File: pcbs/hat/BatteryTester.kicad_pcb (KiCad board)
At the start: 2 copper layers, 30 parts, among them J1 Screw_Terminal_01x02, J2 Conn_01x02_Female, J3 Conn_01x02_Female, J4 Conn_01x02_Female, J5 Conn_01x02_Female, J6 Conn_01x02_Female, J7 Conn_01x02_Female, J8 Conn_01x02_Female, J9 Conn_01x02_Female, U1 NUCLEO-F401RE, U18 MCP3008, U19 MCP3008, U20 MCP3008, U21 ???

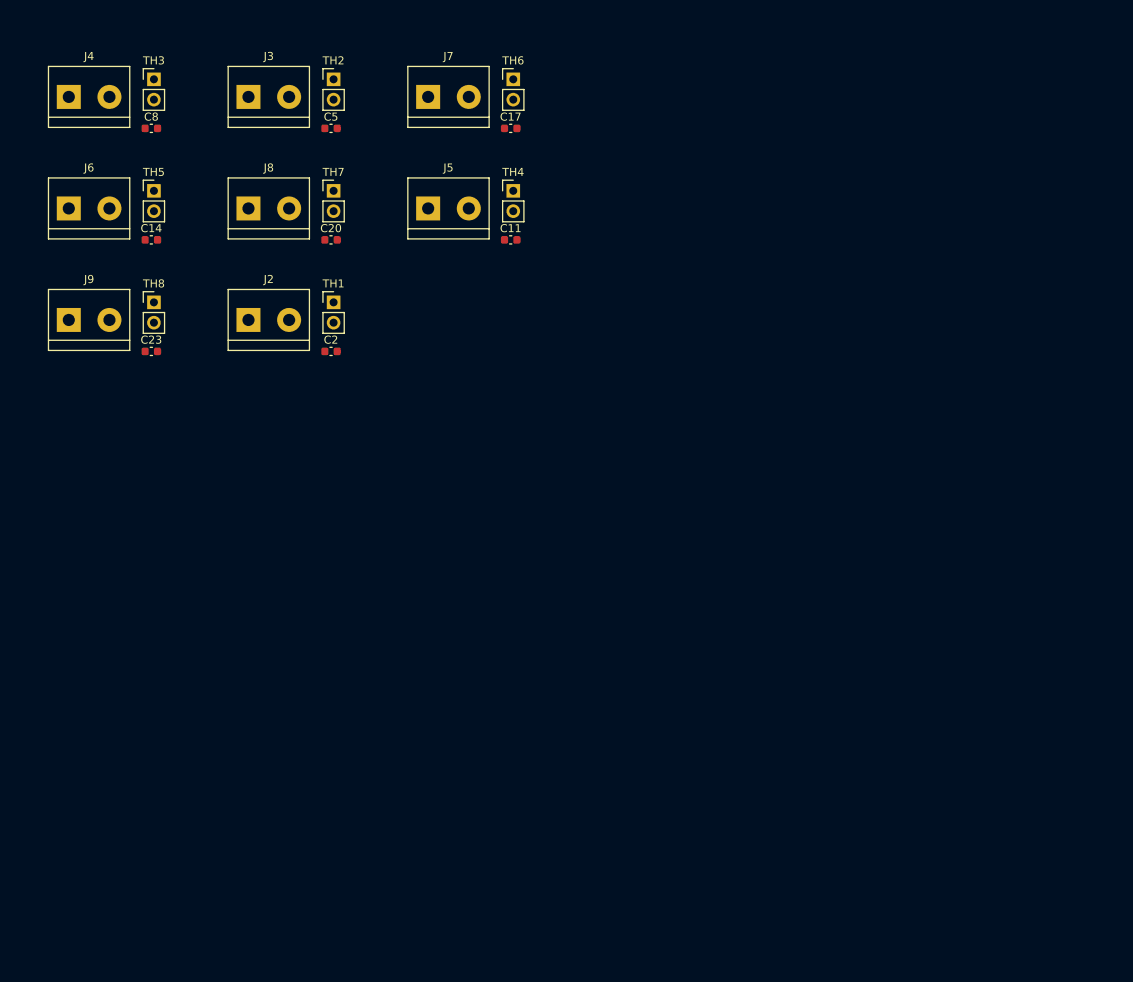
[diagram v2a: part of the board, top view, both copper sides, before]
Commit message: select parts for current and temperature sensors
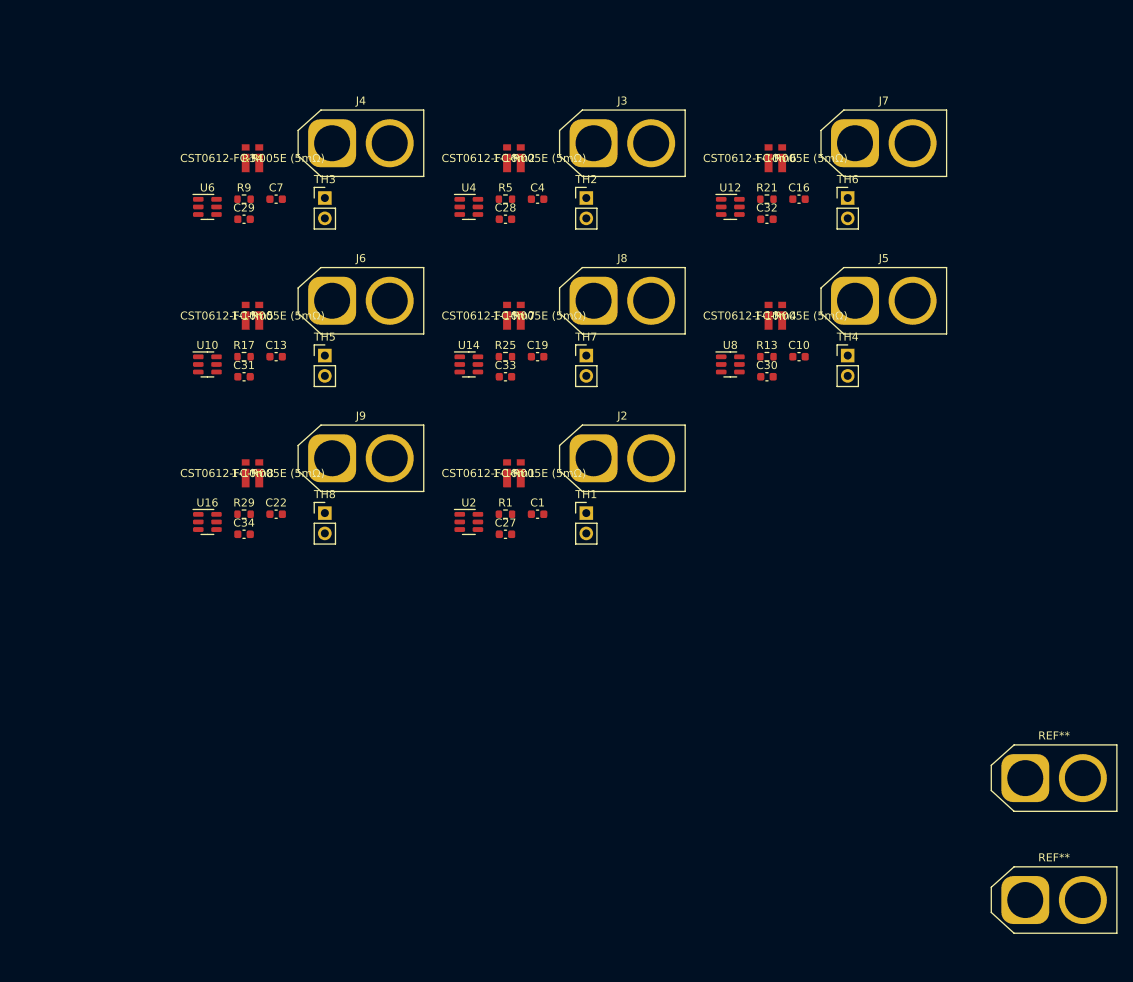
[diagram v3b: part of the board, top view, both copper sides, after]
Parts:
- removed C11, C14, C17, C2, C20, C23, C5, C8: C, Capacitor_SMD:C_0603_1608Metric
- added 1-10m1: CST0612-FC-R005E (5mΩ), STS_Resistor_SMD:CST0612-FC-R002E, F.Cu at (185.4, 83.8)
- added 1-10m2: CST0612-FC-R005E (5mΩ), STS_Resistor_SMD:CST0612-FC-R002E, F.Cu at (185.4, 44.4)
- added 1-10m4: CST0612-FC-R005E (5mΩ), STS_Resistor_SMD:CST0612-FC-R002E, F.Cu at (218.1, 64.1)
- added 1-10m5: CST0612-FC-R005E (5mΩ), STS_Resistor_SMD:CST0612-FC-R002E, F.Cu at (152.7, 64.1)
- added 1-10m6: CST0612-FC-R005E (5mΩ), STS_Resistor_SMD:CST0612-FC-R002E, F.Cu at (218.1, 44.4)
- added 1-10m7: CST0612-FC-R005E (5mΩ), STS_Resistor_SMD:CST0612-FC-R002E, F.Cu at (185.4, 64.1)
- added 1-10m8: CST0612-FC-R005E (5mΩ), STS_Resistor_SMD:CST0612-FC-R002E, F.Cu at (152.7, 83.8)
- added C1: 1µ, Capacitor_SMD:C_0603_1608Metric, F.Cu at (188.4, 88.9)
- added C10: 1µ, Capacitor_SMD:C_0603_1608Metric, F.Cu at (221.1, 69.2)
- added C13: 1µ, Capacitor_SMD:C_0603_1608Metric, F.Cu at (155.7, 69.2)
- added C16: 1µ, Capacitor_SMD:C_0603_1608Metric, F.Cu at (221.1, 49.6)
- added C19: 1µ, Capacitor_SMD:C_0603_1608Metric, F.Cu at (188.4, 69.2)
- added C22: 1µ, Capacitor_SMD:C_0603_1608Metric, F.Cu at (155.7, 88.9)
- added C27: 100n, Capacitor_SMD:C_0603_1608Metric, F.Cu at (184.4, 91.4)
- added C28: 100n, Capacitor_SMD:C_0603_1608Metric, F.Cu at (184.4, 52.1)
- added C29: 100n, Capacitor_SMD:C_0603_1608Metric, F.Cu at (151.7, 52.1)
- added C30: 100n, Capacitor_SMD:C_0603_1608Metric, F.Cu at (217.0, 71.8)
- added C31: 100n, Capacitor_SMD:C_0603_1608Metric, F.Cu at (151.7, 71.8)
- added C32: 100n, Capacitor_SMD:C_0603_1608Metric, F.Cu at (217.0, 52.1)
- added C33: 100n, Capacitor_SMD:C_0603_1608Metric, F.Cu at (184.4, 71.8)
- added C34: 100n, Capacitor_SMD:C_0603_1608Metric, F.Cu at (151.7, 91.4)
- added C4: 1µ, Capacitor_SMD:C_0603_1608Metric, F.Cu at (188.4, 49.6)
- added C7: 1µ, Capacitor_SMD:C_0603_1608Metric, F.Cu at (155.7, 49.6)
- added R1: 3k3, Resistor_SMD:R_0603_1608Metric, F.Cu at (184.4, 88.9)
- added R13: 3k3, Resistor_SMD:R_0603_1608Metric, F.Cu at (217.0, 69.2)
- added R17: 3k3, Resistor_SMD:R_0603_1608Metric, F.Cu at (151.7, 69.2)
- added R21: 3k3, Resistor_SMD:R_0603_1608Metric, F.Cu at (217.0, 49.6)
- added R25: 3k3, Resistor_SMD:R_0603_1608Metric, F.Cu at (184.4, 69.2)
- added R29: 3k3, Resistor_SMD:R_0603_1608Metric, F.Cu at (151.7, 88.9)
- added R34: CST0612-FC-R005E (5mΩ), STS_Resistor_SMD:CST0612-FC-R002E, F.Cu at (152.7, 44.4)
- added R5: 3k3, Resistor_SMD:R_0603_1608Metric, F.Cu at (184.4, 49.6)
- added R9: 3k3, Resistor_SMD:R_0603_1608Metric, F.Cu at (151.7, 49.6)
- added REF**: AMASS_XT60-F_1x02_P7.20mm_Vertical, Connector_AMASS:AMASS_XT60-F_1x02_P7.20mm_Vertical, F.Cu at (249.3, 121.9)
- added REF**: AMASS_XT60-M_1x02_P7.20mm_Vertical, Connector_AMASS:AMASS_XT60-M_1x02_P7.20mm_Vertical, F.Cu at (249.3, 137.2)
- added U10: INA181A4IDBVR, Package_TO_SOT_SMD:SOT-23-6, F.Cu at (147.1, 70.2)
- added U12: INA181A4IDBVR, Package_TO_SOT_SMD:SOT-23-6, F.Cu at (212.5, 50.5)
- added U14: INA181A4IDBVR, Package_TO_SOT_SMD:SOT-23-6, F.Cu at (179.8, 70.2)
- added U16: INA181A4IDBVR, Package_TO_SOT_SMD:SOT-23-6, F.Cu at (147.1, 89.9)
- added U2: INA181A4IDBVR, Package_TO_SOT_SMD:SOT-23-6, F.Cu at (179.8, 89.9)
- added U4: INA181A4IDBVR, Package_TO_SOT_SMD:SOT-23-6, F.Cu at (179.8, 50.5)
- added U6: INA181A4IDBVR, Package_TO_SOT_SMD:SOT-23-6, F.Cu at (147.1, 50.5)
- added U8: INA181A4IDBVR, Package_TO_SOT_SMD:SOT-23-6, F.Cu at (212.5, 70.2)
- J2, J3, J4, J5, J6, J7, J8, J9: value Conn_01x02_Female -> XT60; footprint TerminalBlock:TerminalBlock_bornier-2_P5.08mm -> Connector_AMASS:AMASS_XT60-M_1x02_P7.20mm_Vertical
- TH1, TH2, TH3, TH4, TH5, TH6, TH7, TH8: value Thermistor_NTC -> Thermistor_NTC_10k
- moved J5 54.6 mm to (228.1, 62.3)
- moved J7 53.7 mm to (228.1, 42.6)
- moved TH4 46.6 mm to (227.1, 69.1)
- moved J2 46.5 mm to (195.4, 81.9)
- moved J8 44.7 mm to (195.4, 62.3)
- moved TH6 44.4 mm to (227.1, 49.4)
- moved J3 43.5 mm to (195.4, 42.6)
- moved TH1 41.1 mm to (194.5, 88.8)
- moved TH7 37.7 mm to (194.5, 69.1)
- moved J9 37.2 mm to (162.7, 81.9)
- moved TH2 34.9 mm to (194.5, 49.4)
- moved J6 34.9 mm to (162.7, 62.3)
- moved TH8 33.9 mm to (161.8, 88.8)
- moved J4 33.4 mm to (162.7, 42.6)
- moved TH5 29.7 mm to (161.8, 69.1)
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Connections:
- J2 pad 1: Net-(1-10m1-Pad1) -> /test-battery-1/VBAT
- J2 pad 2: /test-battery-1/VBAT -> /test-battery-1/GNDBAT
- J3 pad 1: Net-(1-10m2-Pad1) -> /test-battery-2/VBAT
- J3 pad 2: /test-battery-2/VBAT -> /test-battery-2/GNDBAT
- J4 pad 1: Net-(1-10m3-Pad1) -> /test-battery-3/VBAT
- J4 pad 2: /test-battery-3/VBAT -> /test-battery-3/GNDBAT
- J5 pad 1: Net-(1-10m4-Pad1) -> /test-battery-4/VBAT
- J5 pad 2: /test-battery-4/VBAT -> /test-battery-4/GNDBAT
- J6 pad 1: Net-(1-10m5-Pad1) -> /test-battery-5/VBAT
- J6 pad 2: /test-battery-5/VBAT -> /test-battery-5/GNDBAT
- J7 pad 1: Net-(1-10m6-Pad1) -> /test-battery-8/VBAT
- J7 pad 2: /test-battery-8/VBAT -> /test-battery-8/GNDBAT
- J8 pad 1: Net-(1-10m7-Pad1) -> /test-battery-7/VBAT
- J8 pad 2: /test-battery-7/VBAT -> /test-battery-7/GNDBAT
- J9 pad 1: Net-(1-10m8-Pad1) -> /test-battery-6/VBAT
- J9 pad 2: /test-battery-6/VBAT -> /test-battery-6/GNDBAT
- U21 pad 3: unconnected-(U21-Pad3) -> GND

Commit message: work on charging circuit
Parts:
- removed REF**: AMASS_XT60-F_1x02_P7.20mm_Vertical, Connector_AMASS:AMASS_XT60-F_1x02_P7.20mm_Vertical
- removed REF**: AMASS_XT60-M_1x02_P7.20mm_Vertical, Connector_AMASS:AMASS_XT60-M_1x02_P7.20mm_Vertical
- added C12: 1µ, Capacitor_SMD:C_0603_1608Metric, F.Cu at (225.1, 83.8)
- added C15: 1µ, Capacitor_SMD:C_0603_1608Metric, F.Cu at (124.5, 83.8)
- added C18: 1µ, Capacitor_SMD:C_0603_1608Metric, F.Cu at (225.1, 53.3)
- added C21: 1µ, Capacitor_SMD:C_0603_1608Metric, F.Cu at (174.8, 83.8)
- added C24: 1µ, Capacitor_SMD:C_0603_1608Metric, F.Cu at (124.5, 114.3)
- added C3: 1µ, Capacitor_SMD:C_0603_1608Metric, F.Cu at (174.8, 114.3)
- added C6: 1µ, Capacitor_SMD:C_0603_1608Metric, F.Cu at (174.8, 53.3)
- added C9: 1µ, Capacitor_SMD:C_0603_1608Metric, F.Cu at (124.5, 53.3)
- added R11: 10k, Resistor_SMD:R_0603_1608Metric, F.Cu at (163.6, 31.9)
- added R12: 3k3, Resistor_SMD:R_0603_1608Metric, F.Cu at (163.6, 29.4)
- added R15: 10k, Resistor_SMD:R_0603_1608Metric, F.Cu at (264.2, 62.4)
- added R16: 3k3, Resistor_SMD:R_0603_1608Metric, F.Cu at (264.2, 59.9)
- added R19: 10k, Resistor_SMD:R_0603_1608Metric, F.Cu at (163.6, 62.4)
- added R20: 3k3, Resistor_SMD:R_0603_1608Metric, F.Cu at (163.6, 59.9)
- added R23: 10k, Resistor_SMD:R_0603_1608Metric, F.Cu at (264.2, 31.9)
- added R24: 3k3, Resistor_SMD:R_0603_1608Metric, F.Cu at (264.2, 29.4)
- added R27: 10k, Resistor_SMD:R_0603_1608Metric, F.Cu at (213.9, 62.4)
- added R28: 3k3, Resistor_SMD:R_0603_1608Metric, F.Cu at (213.9, 59.9)
- added R3: 10k, Resistor_SMD:R_0603_1608Metric, F.Cu at (213.9, 92.9)
- added R31: 10k, Resistor_SMD:R_0603_1608Metric, F.Cu at (163.6, 92.9)
- added R32: 3k3, Resistor_SMD:R_0603_1608Metric, F.Cu at (163.6, 90.4)
- added R35: 680, Resistor_SMD:R_0603_1608Metric, F.Cu at (209.2, 97.6)
- added R36: 10k, Resistor_SMD:R_0603_1608Metric, F.Cu at (206.6, 100.7)
- added R37: 680, Resistor_SMD:R_0603_1608Metric, F.Cu at (209.2, 36.6)
- added R38: 10k, Resistor_SMD:R_0603_1608Metric, F.Cu at (206.6, 39.7)
- added R39: 680, Resistor_SMD:R_0603_1608Metric, F.Cu at (158.9, 36.6)
- added R4: 3k3, Resistor_SMD:R_0603_1608Metric, F.Cu at (213.9, 90.4)
- added R40: 10k, Resistor_SMD:R_0603_1608Metric, F.Cu at (156.3, 39.7)
- added R41: 680, Resistor_SMD:R_0603_1608Metric, F.Cu at (259.6, 67.1)
- added R42: 10k, Resistor_SMD:R_0603_1608Metric, F.Cu at (256.9, 70.2)
- added R43: 680, Resistor_SMD:R_0603_1608Metric, F.Cu at (158.9, 67.1)
- added R44: 10k, Resistor_SMD:R_0603_1608Metric, F.Cu at (156.3, 70.2)
- added R45: 680, Resistor_SMD:R_0603_1608Metric, F.Cu at (259.6, 36.6)
- added R46: 10k, Resistor_SMD:R_0603_1608Metric, F.Cu at (256.9, 39.7)
- added R47: 680, Resistor_SMD:R_0603_1608Metric, F.Cu at (209.2, 67.1)
- added R48: 10k, Resistor_SMD:R_0603_1608Metric, F.Cu at (206.6, 70.2)
- added R49: 680, Resistor_SMD:R_0603_1608Metric, F.Cu at (158.9, 97.6)
- added R50: 10k, Resistor_SMD:R_0603_1608Metric, F.Cu at (156.3, 100.7)
- added R7: 10k, Resistor_SMD:R_0603_1608Metric, F.Cu at (213.9, 31.9)
- added R8: 3k3, Resistor_SMD:R_0603_1608Metric, F.Cu at (213.9, 29.4)
- added U11: TP5000_Breakout_Akaddy, STS_Boards:TP5000_Breakout_Akaddy, F.Cu at (126.2, 80.1)
- added U13: TP5000_Breakout_Akaddy, STS_Boards:TP5000_Breakout_Akaddy, F.Cu at (226.8, 49.6)
- added U15: TP5000_Breakout_Akaddy, STS_Boards:TP5000_Breakout_Akaddy, F.Cu at (176.5, 80.1)
- added U17: TP5000_Breakout_Akaddy, STS_Boards:TP5000_Breakout_Akaddy, F.Cu at (126.2, 110.6)
- added U3: TP5000_Breakout_Akaddy, STS_Boards:TP5000_Breakout_Akaddy, F.Cu at (176.5, 110.6)
- added U5: TP5000_Breakout_Akaddy, STS_Boards:TP5000_Breakout_Akaddy, F.Cu at (176.5, 49.6)
- added U7: TP5000_Breakout_Akaddy, STS_Boards:TP5000_Breakout_Akaddy, F.Cu at (126.2, 49.6)
- added U9: TP5000_Breakout_Akaddy, STS_Boards:TP5000_Breakout_Akaddy, F.Cu at (226.8, 80.1)
- moved TH6 37.8 mm to (259.9, 30.5)
- moved C22 35.2 mm to (132.5, 115.4)
- moved R29 34.4 mm to (128.5, 114.3)
- moved TH4 33.7 mm to (259.9, 61.0)
- moved 1-10m4 32.1 mm to (248.2, 75.3)
- moved U8 32.1 mm to (242.6, 81.4)
- moved 1-10m6 30.1 mm to (248.2, 44.8)
- moved U12 30.1 mm to (242.6, 50.9)
- moved C13 28.0 mm to (132.5, 84.9)
- moved C34 27.5 mm to (136.5, 114.3)
- moved R17 27.4 mm to (128.5, 83.8)
- moved C1 27.0 mm to (182.8, 115.4)
- moved R1 26.0 mm to (178.8, 114.3)
- moved 1-10m1 25.3 mm to (197.9, 105.8)
- moved U2 25.3 mm to (192.3, 111.9)
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
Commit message: more work on charging circuit
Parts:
- removed 1-10m1, 1-10m2, 1-10m4, 1-10m5, 1-10m6, 1-10m7, 1-10m8: CST0612-FC-R005E (5mΩ), STS_Resistor_SMD:CST0612-FC-R002E
- removed C10, C15: 1µ, Capacitor_SMD:C_0603_1608Metric
- removed C30: 100n, Capacitor_SMD:C_0603_1608Metric
- added C11: 100n, Capacitor_SMD:C_0603_1608Metric, F.Cu at (125.3, 44.5)
- added C14: 1µ, Capacitor_SMD:C_0603_1608Metric, F.Cu at (143.8, 29.8)
- added C17: 100n, Capacitor_SMD:C_0603_1608Metric, F.Cu at (239.6, 62.7)
- added C2: 100n, Capacitor_SMD:C_0603_1608Metric, F.Cu at (178.5, 98.4)
- added C23: 220u, Capacitor_THT:CP_Radial_D6.3mm_P2.50mm, F.Cu at (118.2, 78.4)
- added C26: 100n, Capacitor_SMD:C_0603_1608Metric, F.Cu at (247.5, 44.5)
- added C36: 100n, Capacitor_SMD:C_0603_1608Metric, F.Cu at (125.3, 115.8)
- added C37: 100n, Capacitor_SMD:C_0603_1608Metric, F.Cu at (117.4, 98.4)
- added C38: 220u, Capacitor_THT:CP_Radial_D6.3mm_P2.50mm, F.Cu at (118.2, 114.0)
- added C39: 1µ, Capacitor_SMD:C_0603_1608Metric, F.Cu at (143.8, 101.1)
- added C8: 220u, Capacitor_THT:CP_Radial_D6.3mm_P2.50mm, F.Cu at (179.3, 42.7)
- added Q1: Q_NMOS_DGS, Package_TO_SOT_THT:TO-220-3_Vertical, F.Cu at (194.6, 103.8)
- added Q10: Q_NMOS_DGS, Package_TO_SOT_SMD:SOT-223, F.Cu at (150.3, 58.1)
- added Q11: Q_NMOS_DGS, Package_TO_SOT_THT:TO-220-3_Vertical, F.Cu at (255.7, 32.4)
- added Q12: Q_NMOS_DGS, Package_TO_SOT_SMD:SOT-223, F.Cu at (272.5, 22.4)
- added Q13: Q_NMOS_DGS, Package_TO_SOT_THT:TO-220-3_Vertical, F.Cu at (194.6, 68.1)
- added Q14: Q_NMOS_DGS, Package_TO_SOT_SMD:SOT-223, F.Cu at (211.4, 58.1)
- added Q15: Q_NMOS_DGS, Package_TO_SOT_THT:TO-220-3_Vertical, F.Cu at (133.5, 103.8)
- added Q16: Q_NMOS_DGS, Package_TO_SOT_SMD:SOT-223, F.Cu at (150.3, 93.7)
- added Q2: Q_NMOS_DGS, Package_TO_SOT_SMD:SOT-223, F.Cu at (211.4, 93.7)
- added Q3: Q_NMOS_DGS, Package_TO_SOT_THT:TO-220-3_Vertical, F.Cu at (194.6, 32.4)
- added Q4: Q_NMOS_DGS, Package_TO_SOT_SMD:SOT-223, F.Cu at (211.4, 22.4)
- added Q5: Q_NMOS_DGS, Package_TO_SOT_THT:TO-220-3_Vertical, F.Cu at (133.5, 32.4)
- added Q6: Q_NMOS_DGS, Package_TO_SOT_SMD:SOT-223, F.Cu at (150.3, 22.4)
- added Q7: Q_NMOS_DGS, Package_TO_SOT_THT:TO-220-3_Vertical, F.Cu at (255.7, 68.1)
- added Q8: Q_NMOS_DGS, Package_TO_SOT_SMD:SOT-223, F.Cu at (272.5, 58.1)
- added Q9: Q_NMOS_DGS, Package_TO_SOT_THT:TO-220-3_Vertical, F.Cu at (133.5, 68.1)
- added R10: 1, Resistor_THT:R_Axial_DIN0617_L17.0mm_D6.0mm_P25.40mm_Horizontal, F.Cu at (161.5, 22.0)
- added R14: 10k, Resistor_SMD:R_0603_1608Metric, F.Cu at (190.4, 44.5)
- added R18: 1, Resistor_THT:R_Axial_DIN0617_L17.0mm_D6.0mm_P25.40mm_Horizontal, F.Cu at (100.4, 22.0)
- added R2: 1, Resistor_THT:R_Axial_DIN0617_L17.0mm_D6.0mm_P25.40mm_Horizontal, F.Cu at (161.5, 93.4)
- added R22: 10k, Resistor_SMD:R_0603_1608Metric, F.Cu at (129.3, 44.5)
- added R26: 1, Resistor_THT:R_Axial_DIN0617_L17.0mm_D6.0mm_P25.40mm_Horizontal, F.Cu at (222.6, 57.7)
- added R30: 10k, Resistor_SMD:R_0603_1608Metric, F.Cu at (251.5, 80.1)
- added R33: CST0612-FC-R005E (5mΩ), STS_Resistor_SMD:CST0612-FC-R002E, F.Cu at (123.6, 70.6)
- added R51: 680, Resistor_SMD:R_0603_1608Metric, F.Cu at (186.5, 62.7)
- added R52: 10k, Resistor_SMD:R_0603_1608Metric, F.Cu at (182.5, 83.5)
- added R53: 3k3, Resistor_SMD:R_0603_1608Metric, F.Cu at (178.5, 83.5)
- added R54: 10k, Resistor_SMD:R_0603_1608Metric, F.Cu at (190.4, 80.1)
- added R55: 680, Resistor_SMD:R_0603_1608Metric, F.Cu at (198.0, 71.4)
- added R56: 10k, Resistor_SMD:R_0603_1608Metric, F.Cu at (182.5, 62.7)
- added R57: CST0612-FC-R005E (5mΩ), STS_Resistor_SMD:CST0612-FC-R002E, F.Cu at (123.6, 106.3)
- added R58: 1, Resistor_THT:R_Axial_DIN0617_L17.0mm_D6.0mm_P25.40mm_Horizontal, F.Cu at (100.4, 93.4)
- added R59: 680, Resistor_SMD:R_0603_1608Metric, F.Cu at (125.4, 98.4)
- added R6: 10k, Resistor_SMD:R_0603_1608Metric, F.Cu at (190.4, 115.8)
- added R60: 10k, Resistor_SMD:R_0603_1608Metric, F.Cu at (121.4, 119.2)
- added R61: 3k3, Resistor_SMD:R_0603_1608Metric, F.Cu at (117.4, 119.2)
- added R62: 10k, Resistor_SMD:R_0603_1608Metric, F.Cu at (129.3, 115.8)
- added R63: 680, Resistor_SMD:R_0603_1608Metric, F.Cu at (136.9, 107.1)
- added R64: 10k, Resistor_SMD:R_0603_1608Metric, F.Cu at (121.4, 98.4)
- C1, C12, C16, C21, C22, C6, C7: value 1µ -> 100n
- C13, C18, C3: value 1µ -> 220u; footprint Capacitor_SMD:C_0603_1608Metric -> Capacitor_THT:CP_Radial_D6.3mm_P2.50mm
- C28, C33: value 100n -> 220u; footprint Capacitor_SMD:C_0603_1608Metric -> Capacitor_THT:CP_Radial_D6.3mm_P2.50mm
- C29, C34: value 100n -> 1µ
- R1, R17, R25, R9: value 3k3 -> CST0612-FC-R005E (5mΩ); footprint Resistor_SMD:R_0603_1608Metric -> STS_Resistor_SMD:CST0612-FC-R002E
- R11, R15, R19, R23, R27, R3, R31, R7: value 10k -> 680
- R12, R16, R20, R24, R28, R32, R4, R8: value 3k3 -> 10k
- R34: value CST0612-FC-R005E (5mΩ) -> 1; footprint STS_Resistor_SMD:CST0612-FC-R002E -> Resistor_THT:R_Axial_DIN0617_L17.0mm_D6.0mm_P25.40mm_Horizontal
- R37, R45: value 680 -> 3k3
- R41, R49: value 680 -> CST0612-FC-R005E (5mΩ); footprint Resistor_SMD:R_0603_1608Metric -> STS_Resistor_SMD:CST0612-FC-R002E
- R42, R50: value 10k -> 1; footprint Resistor_SMD:R_0603_1608Metric -> Resistor_THT:R_Axial_DIN0617_L17.0mm_D6.0mm_P25.40mm_Horizontal
- U1: value NUCLEO-F401RE -> INA181A4IDBVR; footprint STS_Boards:ST_Morpho_Connector_64_MountingHoles -> Package_TO_SOT_SMD:SOT-23-6
- U10, U12, U14, U16, U2, U4, U6, U8: value INA181A4IDBVR -> TP5000_Breakout_Akaddy; footprint Package_TO_SOT_SMD:SOT-23-6 -> STS_Boards:TP5000_Breakout_Akaddy
- U11, U13, U15, U3, U5, U7, U9: value TP5000_Breakout_Akaddy -> INA181A4IDBVR; footprint STS_Boards:TP5000_Breakout_Akaddy -> Package_TO_SOT_SMD:SOT-23-6
- U17: value TP5000_Breakout_Akaddy -> NUCLEO-F401RE; footprint STS_Boards:TP5000_Breakout_Akaddy -> STS_Boards:ST_Morpho_Connector_64_MountingHoles
- moved R24 142.9 mm to (121.4, 27.1)
- moved C29 131.7 mm to (266.0, 29.8)
- moved U1 129.1 mm to (187.0, 112.3)
- moved U11 128.1 mm to (248.1, 41.0)
- moved R23 127.3 mm to (136.9, 35.7)
- moved U7 124.9 mm to (248.1, 76.7)
- moved C12 121.8 mm to (117.4, 27.1)
- moved R29 115.3 mm to (239.6, 83.5)
- moved R21 111.9 mm to (117.4, 47.9)
- moved R37 103.2 mm to (117.4, 83.5)
- moved C27 102.0 mm to (239.6, 27.1)
- moved U9 100.9 mm to (125.9, 76.7)
- moved R31 97.9 mm to (259.1, 71.4)
- moved R43 97.3 mm to (247.6, 27.1)
- moved R35 90.8 mm to (125.4, 62.7)
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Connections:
- C1 pad 2: /SENSOR_11 -> +5V
- C12 pad 1: GND -> Net-(C12-Pad1)
- C12 pad 2: /SENSOR_40 -> GND
- C13 pad 1: GND -> Net-(C13-Pad1)
- C13 pad 2: /SENSOR_51 -> GND
- C16 pad 2: /SENSOR_81 -> +5V
- C18 pad 1: GND -> Net-(C18-Pad1)
- C18 pad 2: /SENSOR_80 -> GND
- C19 pad 2: /SENSOR_71 -> /SENSOR_41
- C21 pad 2: /SENSOR_70 -> +5V
- C22 pad 1: GND -> Net-(C22-Pad1)
- C22 pad 2: /SENSOR_61 -> GND
- C24 pad 2: /SENSOR_60 -> /SENSOR_51
- C27 pad 1: GND -> Net-(C27-Pad1)
- C27 pad 2: +5V -> GND
- C28 pad 1: GND -> Net-(C28-Pad1)
- C28 pad 2: +5V -> GND
- C29 pad 2: +5V -> /SENSOR_81
- C3 pad 1: GND -> Net-(C3-Pad1)
- C3 pad 2: /SENSOR_10 -> GND
- C32 pad 1: GND -> Net-(C32-Pad1)
- C32 pad 2: +5V -> GND
- C33 pad 1: GND -> Net-(C33-Pad1)
- C33 pad 2: +5V -> GND
- C34 pad 2: +5V -> /SENSOR_71
- C4 pad 2: /SENSOR_21 -> /SENSOR_11
- C6 pad 2: /SENSOR_20 -> +5V
- C7 pad 1: GND -> Net-(C7-Pad1)
- C7 pad 2: /SENSOR_31 -> GND
- C9 pad 2: /SENSOR_30 -> /SENSOR_21
- R1 pad 1: Net-(R1-Pad1) -> /test-battery-1/GNDBAT
- R1 pad 2: /SENSOR_11 -> Net-(R1-Pad2)
- R11 pad 1: /SENSOR_32 -> /SIGNAL_21
- R11 pad 2: GND -> Net-(C7-Pad1)
- R12 pad 1: /test-battery-3/VBAT -> Net-(C7-Pad1)
- R12 pad 2: /SENSOR_30 -> GND
- R13 pad 2: /SENSOR_41 -> /SENSOR_21
- R15 pad 1: /SENSOR_42 -> /SIGNAL_20
- R15 pad 2: GND -> Net-(Q4-Pad2)
- R16 pad 1: /test-battery-4/VBAT -> Net-(Q4-Pad2)
- R16 pad 2: /SENSOR_40 -> GND
- R17 pad 1: Net-(R17-Pad1) -> /test-battery-3/GNDBAT
- R17 pad 2: /SENSOR_51 -> Net-(R17-Pad2)
- R19 pad 1: /SENSOR_52 -> /SIGNAL_31
- R19 pad 2: GND -> Net-(C12-Pad1)
- R20 pad 1: /test-battery-5/VBAT -> Net-(C12-Pad1)
- R20 pad 2: /SENSOR_50 -> GND
- R21 pad 2: /SENSOR_81 -> /SENSOR_31
- R23 pad 1: /SENSOR_82 -> /SIGNAL_30
- R23 pad 2: GND -> Net-(Q6-Pad2)
- R24 pad 1: /test-battery-8/VBAT -> Net-(Q6-Pad2)
- R24 pad 2: /SENSOR_80 -> GND
- R25 pad 1: Net-(R25-Pad1) -> /test-battery-4/GNDBAT
- R25 pad 2: /SENSOR_71 -> Net-(R25-Pad2)
- R27 pad 1: /SENSOR_72 -> /SIGNAL_41
- R27 pad 2: GND -> Net-(C17-Pad1)
- R28 pad 1: /test-battery-7/VBAT -> Net-(C17-Pad1)
- R28 pad 2: /SENSOR_70 -> GND
- R29 pad 2: /SENSOR_61 -> /SENSOR_41
- R3 pad 1: /SENSOR_12 -> /SIGNAL_11
- R3 pad 2: GND -> Net-(C2-Pad1)
- R31 pad 1: /SENSOR_62 -> /SIGNAL_40
- R31 pad 2: GND -> Net-(Q8-Pad2)
- R32 pad 1: /test-battery-6/VBAT -> Net-(Q8-Pad2)
- R32 pad 2: /SENSOR_60 -> GND
- R34 pad 1: /test-battery-3/GNDBAT -> Net-(C23-Pad1)
- R34 pad 2: Net-(R34-Pad2) -> /test-battery-5/VBAT
- R35 pad 1: /SIGNAL_10 -> /SIGNAL_51
- R35 pad 2: Net-(Q1-Pad2) -> Net-(C22-Pad1)
- R36 pad 1: Net-(Q1-Pad2) -> Net-(C22-Pad1)
- R37 pad 1: /SIGNAL_20 -> Net-(R37-Pad1)
- R37 pad 2: Net-(Q3-Pad2) -> /SENSOR_51
- R38 pad 1: Net-(Q3-Pad2) -> /SENSOR_52
- R39 pad 1: /SIGNAL_30 -> /SIGNAL_50
- R4 pad 1: /test-battery-1/VBAT -> Net-(C2-Pad1)
- R4 pad 2: /SENSOR_10 -> GND
- R41 pad 1: /SIGNAL_40 -> /test-battery-8/GNDBAT
- R41 pad 2: Net-(Q7-Pad2) -> Net-(R41-Pad2)
- R42 pad 1: Net-(Q7-Pad2) -> Net-(C28-Pad1)
- R42 pad 2: GND -> /test-battery-8/VBAT
- R43 pad 1: /SIGNAL_50 -> /SIGNAL_81
- R43 pad 2: Net-(Q9-Pad2) -> Net-(C27-Pad1)
- R44 pad 1: Net-(Q9-Pad2) -> Net-(C27-Pad1)
- R45 pad 1: /SIGNAL_80 -> Net-(R45-Pad1)
- R45 pad 2: Net-(Q11-Pad2) -> /SENSOR_81
- R46 pad 1: Net-(Q11-Pad2) -> /SENSOR_82
- R47 pad 1: /SIGNAL_70 -> /SIGNAL_80
- R49 pad 1: /SIGNAL_60 -> /test-battery-7/GNDBAT
- R49 pad 2: Net-(Q15-Pad2) -> Net-(R49-Pad2)
- R5 pad 2: /SENSOR_21 -> /SENSOR_11
- R50 pad 1: Net-(Q15-Pad2) -> Net-(C33-Pad1)
- R50 pad 2: GND -> /test-battery-7/VBAT
- R7 pad 1: /SENSOR_22 -> /SIGNAL_10
- R7 pad 2: GND -> Net-(Q2-Pad2)
- R8 pad 1: /test-battery-2/VBAT -> Net-(Q2-Pad2)
- R8 pad 2: /SENSOR_20 -> GND
- R9 pad 1: Net-(R9-Pad1) -> /test-battery-2/GNDBAT
- R9 pad 2: /SENSOR_31 -> Net-(R9-Pad2)
- U10 pad 1: Net-(R17-Pad1) -> VCC
- U10 pad 2: GND -> Net-(Q10-Pad1)
- U10 pad 3: Net-(1-10m5-Pad2) -> /test-battery-5/VBAT
- U10 pad 4: Net-(1-10m5-Pad3) -> Net-(Q10-Pad1)
- U11 pad 1: VCC -> Net-(R45-Pad1)
- U11 pad 2: Net-(Q9-Pad1) -> GND
- U11 pad 3: /test-battery-5/VBAT -> Net-(R41-Pad2)
- U11 pad 4: Net-(Q9-Pad1) -> Net-(R41-Pad3)
- U12 pad 1: Net-(R21-Pad1) -> VCC
- U12 pad 2: GND -> Net-(Q12-Pad1)
- U12 pad 3: Net-(1-10m6-Pad2) -> /test-battery-8/VBAT
- U12 pad 4: Net-(1-10m6-Pad3) -> Net-(Q12-Pad1)
- U13 pad 1: VCC -> Net-(R53-Pad1)
- U13 pad 2: Net-(Q11-Pad1) -> GND
- U13 pad 3: /test-battery-8/VBAT -> Net-(R49-Pad2)
- U13 pad 4: Net-(Q11-Pad1) -> Net-(R49-Pad3)
- U14 pad 1: Net-(R25-Pad1) -> VCC
- U14 pad 2: GND -> Net-(Q14-Pad1)
- U14 pad 3: Net-(1-10m7-Pad2) -> /test-battery-7/VBAT
- U14 pad 4: Net-(1-10m7-Pad3) -> Net-(Q14-Pad1)
- U15 pad 1: VCC -> Net-(R61-Pad1)
- U15 pad 2: Net-(Q13-Pad1) -> GND
- U15 pad 3: /test-battery-7/VBAT -> Net-(R57-Pad2)
- U15 pad 4: Net-(Q13-Pad1) -> Net-(R57-Pad3)
- U16 pad 1: Net-(R29-Pad1) -> VCC
- U16 pad 2: GND -> Net-(Q16-Pad1)
- U16 pad 3: Net-(1-10m8-Pad2) -> /test-battery-6/VBAT
- U16 pad 4: Net-(1-10m8-Pad3) -> Net-(Q16-Pad1)
- U2 pad 1: Net-(R1-Pad1) -> VCC
- U2 pad 2: GND -> Net-(Q2-Pad1)
- U2 pad 3: Net-(1-10m1-Pad2) -> /test-battery-1/VBAT
- U2 pad 4: Net-(1-10m1-Pad3) -> Net-(Q2-Pad1)
- U3 pad 1: VCC -> Net-(R13-Pad1)
- U3 pad 2: Net-(Q1-Pad1) -> GND
- U3 pad 3: /test-battery-1/VBAT -> Net-(R9-Pad2)
- U3 pad 4: Net-(Q1-Pad1) -> Net-(R9-Pad3)
- U4 pad 1: Net-(R5-Pad1) -> VCC
- U4 pad 2: GND -> Net-(Q4-Pad1)
- U4 pad 3: Net-(1-10m2-Pad2) -> /test-battery-2/VBAT
- U4 pad 4: Net-(1-10m2-Pad3) -> Net-(Q4-Pad1)
- U5 pad 1: VCC -> Net-(R21-Pad1)
- U5 pad 2: Net-(Q3-Pad1) -> GND
- U5 pad 3: /test-battery-2/VBAT -> Net-(R17-Pad2)
- U5 pad 4: Net-(Q3-Pad1) -> Net-(R17-Pad3)
- U6 pad 1: Net-(R9-Pad1) -> VCC
- U6 pad 2: GND -> Net-(Q6-Pad1)
- U6 pad 3: Net-(R34-Pad2) -> /test-battery-3/VBAT
- U6 pad 4: Net-(R34-Pad3) -> Net-(Q6-Pad1)
- U7 pad 1: VCC -> Net-(R29-Pad1)
- U7 pad 2: Net-(Q5-Pad1) -> GND
- U7 pad 3: /test-battery-3/VBAT -> Net-(R25-Pad2)
- U7 pad 4: Net-(Q5-Pad1) -> Net-(R25-Pad3)
- U8 pad 1: Net-(R13-Pad1) -> VCC
- U8 pad 2: GND -> Net-(Q8-Pad1)
- U8 pad 3: Net-(1-10m4-Pad2) -> /test-battery-4/VBAT
- U8 pad 4: Net-(1-10m4-Pad3) -> Net-(Q8-Pad1)
- U9 pad 1: VCC -> Net-(R37-Pad1)
- U9 pad 2: Net-(Q7-Pad1) -> GND
- U9 pad 3: /test-battery-4/VBAT -> Net-(R33-Pad2)
- U9 pad 4: Net-(Q7-Pad1) -> Net-(R33-Pad3)
